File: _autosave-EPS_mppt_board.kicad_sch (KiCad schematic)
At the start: 0 parts

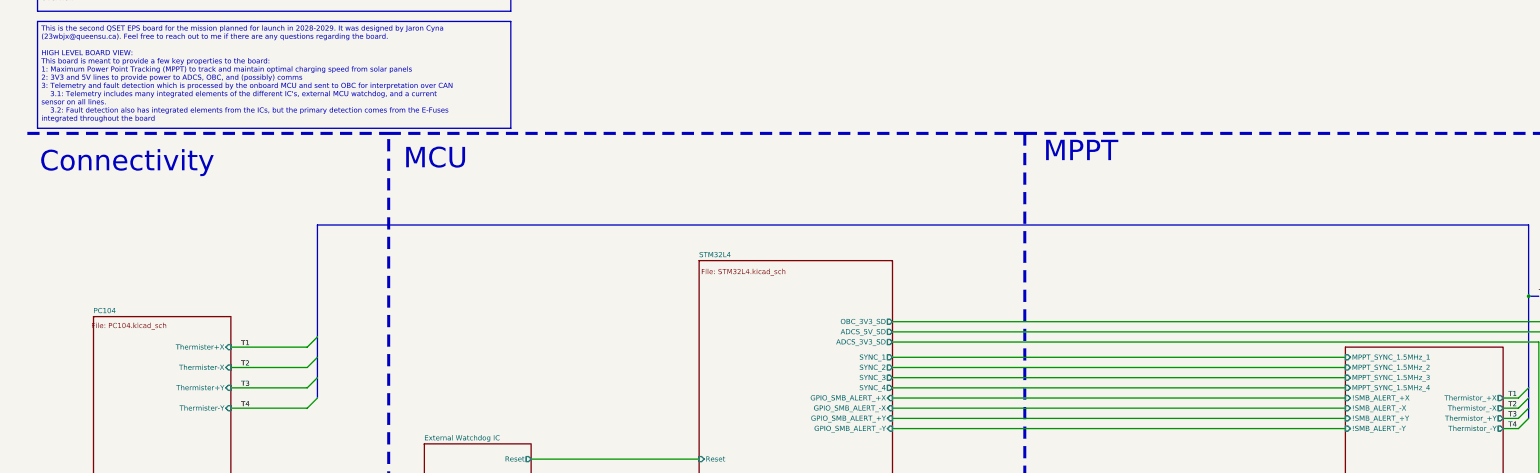
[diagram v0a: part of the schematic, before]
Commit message: Most DRC errors fixed
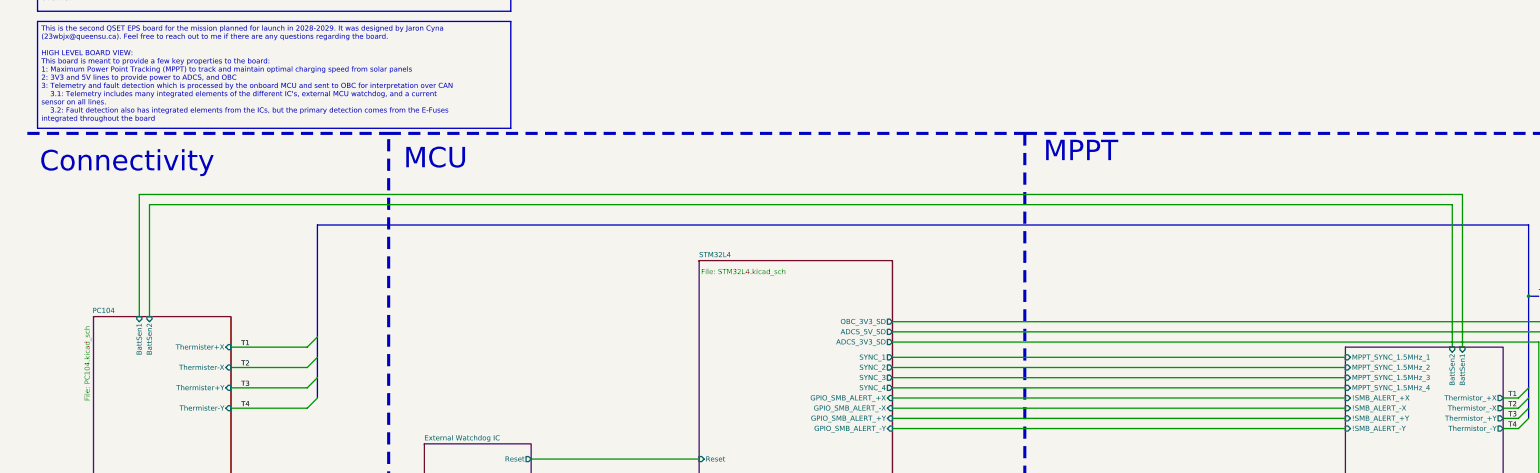
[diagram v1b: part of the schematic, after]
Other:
- sheet MPPT IC ports: added BattSen1, BattSen2; removed none
- sheet PC104 ports: added BattSen1, BattSen2; removed none
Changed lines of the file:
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@@
 		)
 	)
-	(text_box "This is the second QSET EPS board for the mission planned for launch in 2028-2029. It was designed by Jaron Cyna (23wbjx@queensu.ca). Feel free to reach out to me if there are any questions regarding the board.\n\nHIGH LEVEL BOARD VIEW:\nThis board is meant to provide a few key properties to the board:\n1: Maximum Power Point Tracking (MPPT) to track and maintain optimal charging speed from solar panels\n2: 3V3 and 5V lines to provide power to ADCS, OBC, and (possibly) comms\n3: Telemetry and fault detection which is processed by the onboard MCU and sent to OBC for interpretation over CAN\n	3.1: Telemetry includes many integrated elements of the different IC's, external MCU watchdog, and a current sensor on all lines.\n	3.2: Fault detection also has integrated elements from the ICs, but the primary detection comes from the E-Fuses integrated throughout the board"
+	(text_box "This is the second QSET EPS board for the mission planned for launch in 2028-2029. It was designed by Jaron Cyna (23wbjx@queensu.ca). Feel free to reach out to me if there are any questions regarding the board.\n\nHIGH LEVEL BOARD VIEW:\nThis board is meant to provide a few key properties to the board:\n1: Maximum Power Point Tracking (MPPT) to track and maintain optimal charging speed from solar panels\n2: 3V3 and 5V lines to provide power to ADCS, and OBC\n3: Telemetry and fault detection which is processed by the onboard MCU and sent to OBC for interpretation over CAN\n	3.1: Telemetry includes many integrated elements of the different IC's, external MCU watchdog, and a current sensor on all lines.\n	3.2: Fault detection also has integrated elements from the ICs, but the primary detection comes from the E-Fuses integrated throughout the board"
 		(exclude_from_sim no)
 		(at 13.97 22.86 0)
@@
 	(wire
 		(pts
+			(xy 367.03 104.14) (xy 367.03 68.58)
+		)
+		(stroke
+			(width 0)
+			(type default)
+		)
+	)
+	(wire
+		(pts
 			(xy 293.37 148.59) (xy 297.18 148.59)
 		)
@@
 			(type default)
 			(color 57 211 255 1)
+		)
+	)
+	(wire
+		(pts
+			(xy 39.37 96.52) (xy 39.37 66.04)
+		)
+		(stroke
+			(width 0)
+			(type default)
 		)
 	)
@@
 	(wire
 		(pts
+			(xy 39.37 66.04) (xy 369.57 66.04)
+		)
+		(stroke
+			(width 0)
+			(type default)
+		)
+	)
+	(wire
+		(pts
 			(xy 227.33 111.76) (xy 340.36 111.76)
 		)
@@
 	(wire
 		(pts
+			(xy 369.57 66.04) (xy 369.57 104.14)
+		)
+		(stroke
+			(width 0)
+			(type default)
+		)
+	)
+	(wire
+		(pts
 			(xy 402.59 147.32) (xy 379.73 147.32)
 		)
@@
 	(wire
 		(pts
+			(xy 367.03 68.58) (xy 41.91 68.58)
+		)
+		(stroke
+			(width 0)
+			(type default)
+		)
+	)
+	(wire
+		(pts
 			(xy 175.26 229.87) (xy 175.26 243.84)
+		)
+		(stroke
+			(width 0)
+			(type default)
+		)
+	)
+	(wire
+		(pts
+			(xy 41.91 68.58) (xy 41.91 96.52)
 		)
 		(stroke
@@
 		)
 		(property "Sheetname" "PC104"
-			(at 27.94 95.8084 0)
+			(at 27.686 95.758 0)
 			(effects
 				(font
@@
 		)
 		(property "Sheetfile" "PC104.kicad_sch"
-			(at 27.432 98.044 0)
+			(at 25.654 117.602 90)
 			(effects
 				(font
@@
 		(pin "3V3_Out_Batt" input
 			(at 62.23 222.25 0)
+			(effects
+				(font
+					(size 1.27 1.27)
+				)
+				(justify right)
+			)
+		)
+		(pin "BattSen1" input
+			(at 39.37 96.52 90)
+			(effects
+				(font
+					(size 1.27 1.27)
+				)
+				(justify right)
+			)
+		)
+		(pin "BattSen2" input
+			(at 41.91 96.52 90)
 			(effects
 				(font
@@
 			)
 		)
+		(pin "BattSen1" input
+			(at 369.57 104.14 90)
+			(effects
+				(font
+					(size 1.27 1.27)
+				)
+				(justify right)
+			)
+		)
+		(pin "BattSen2" input
+			(at 367.03 104.14 90)
+			(effects
+				(font
+					(size 1.27 1.27)
+				)
+				(justify right)
+			)
+		)
